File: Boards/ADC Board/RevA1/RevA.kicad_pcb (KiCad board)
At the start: 2 copper layers, 85 x 56 mm, 31 parts, among them J1 Left Connector, J10 Jumper Terminals, J11 Arduino Nano, J12 Arduino Nano, J13 Extra Pins, J14 Screw Terminals, J16 Screw Terminals, J2 Right Connector, J3 Screw Terminals, J4 Jumper Terminals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

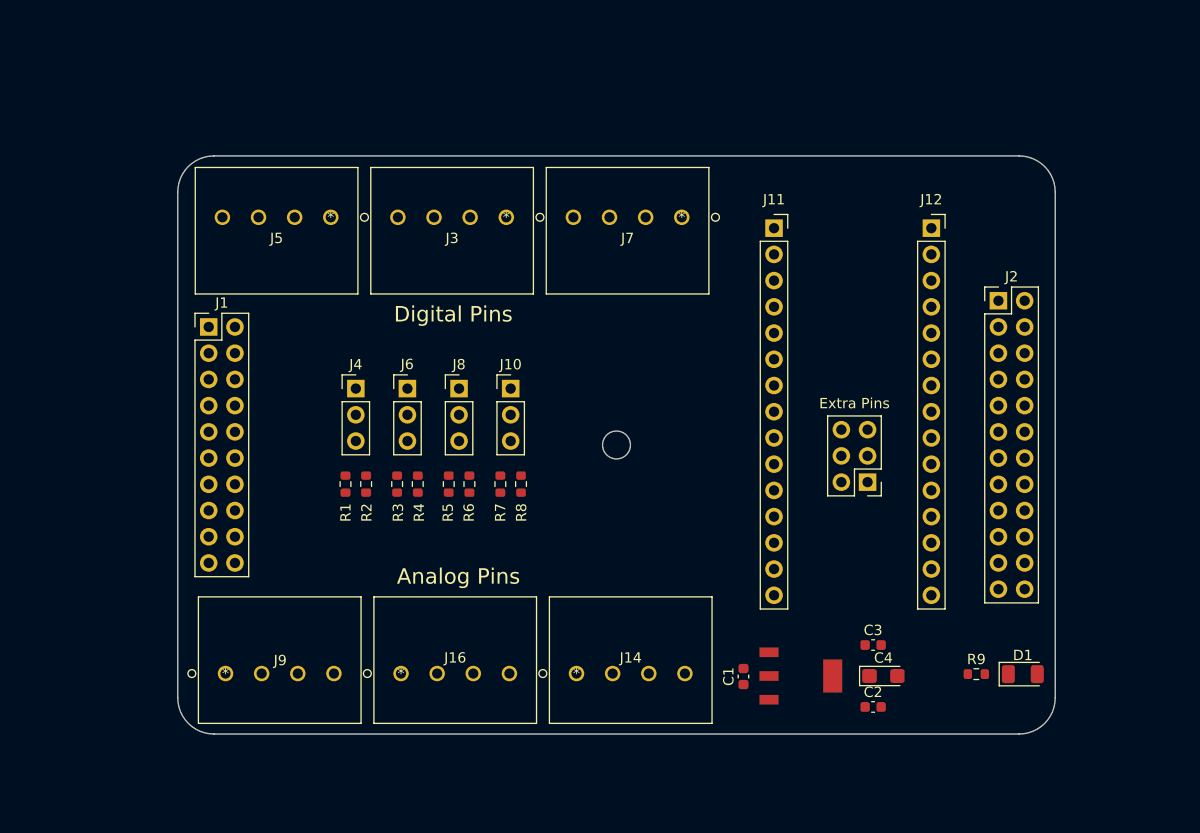
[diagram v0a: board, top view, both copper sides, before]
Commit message: Finished autorouting ADC board and placing text.
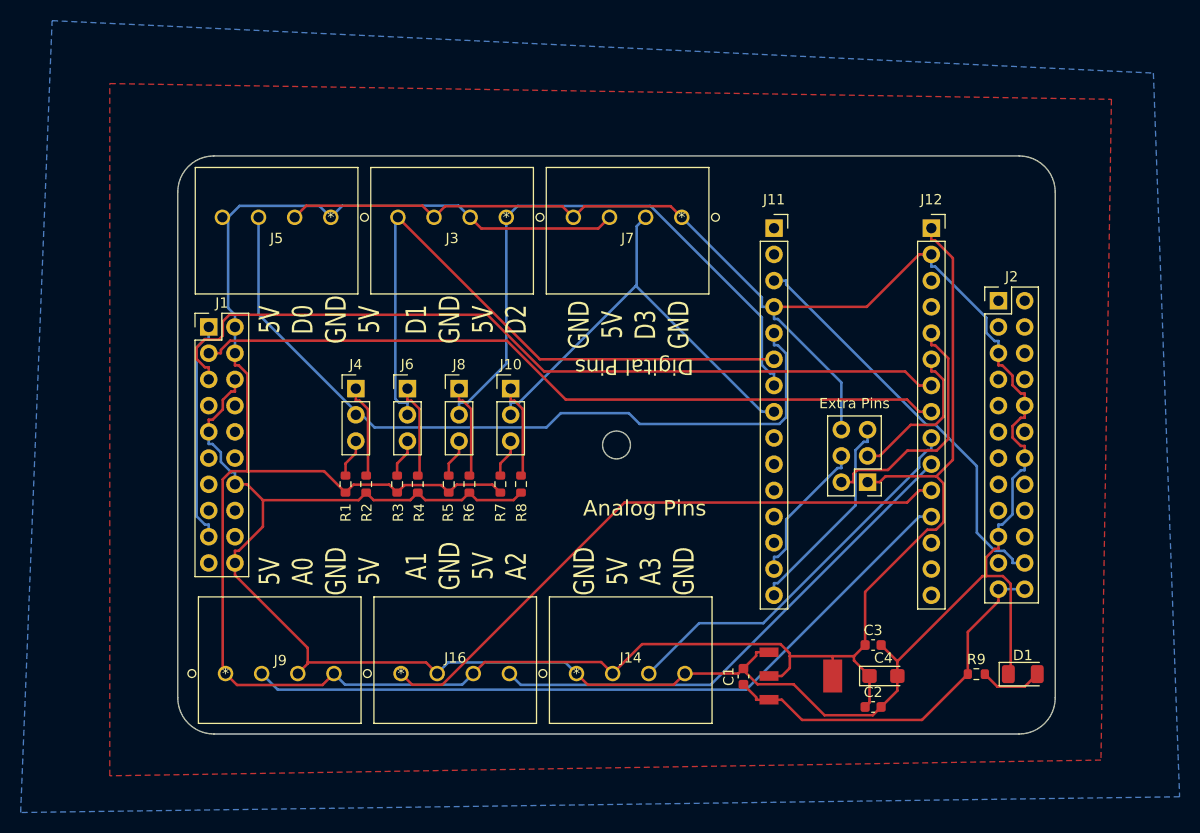
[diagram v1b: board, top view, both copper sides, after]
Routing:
- net /GND: track 0.00 -> 284.3 mm
- net /5V: track 0.00 -> 245.8 mm
- net /I2C_Clock: track 0.00 -> 79.9 mm
- net /Digital_0: track 0.00 -> 75.8 mm
- net /I2C_Data: track 0.00 -> 73.5 mm
- net /Analog_0: track 0.00 -> 72.5 mm
- net /Digital_1: track 0.00 -> 62.3 mm
- net /Analog_1: track 0.00 -> 59.6 mm
- net /Digital_2: track 0.00 -> 58.5 mm
- net /Analog_2: track 0.00 -> 50.2 mm
- net /Digital_3: track 0.00 -> 43.5 mm
- net /Reset: track 0.00 -> 39.8 mm
- net /Analog_3: track 0.00 -> 38.0 mm
- net /VCC: track 0.00 -> 37.1 mm
- net /Controller/A7: track 0.00 -> 23.7 mm
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- added copper zone on B.Cu, net /GND
- added copper zone on F.Cu, net /GND
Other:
- board text added: "5V"
- board text added: "5V A0 GND 5V"
- board text added: "5V D0 GND 5V"
- board text added: "A0"
- board text added: "A1"
- board text added: "A1 GND 5V A2"
- board text added: "A2"
- board text added: "A3"
- board text added: "D0"
- board text added: "D1"
- board text added: "D1 GND 5V D2"
- board text added: "D2"
- board text added: "D3"
- board text added: "GND"
- board text added: "GND 5V A3 GND"
- board text added: "GND 5V D3 GND"

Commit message: In process of updating ADC board to remove 5V connection from PI. Also commiting small changes to uV board.
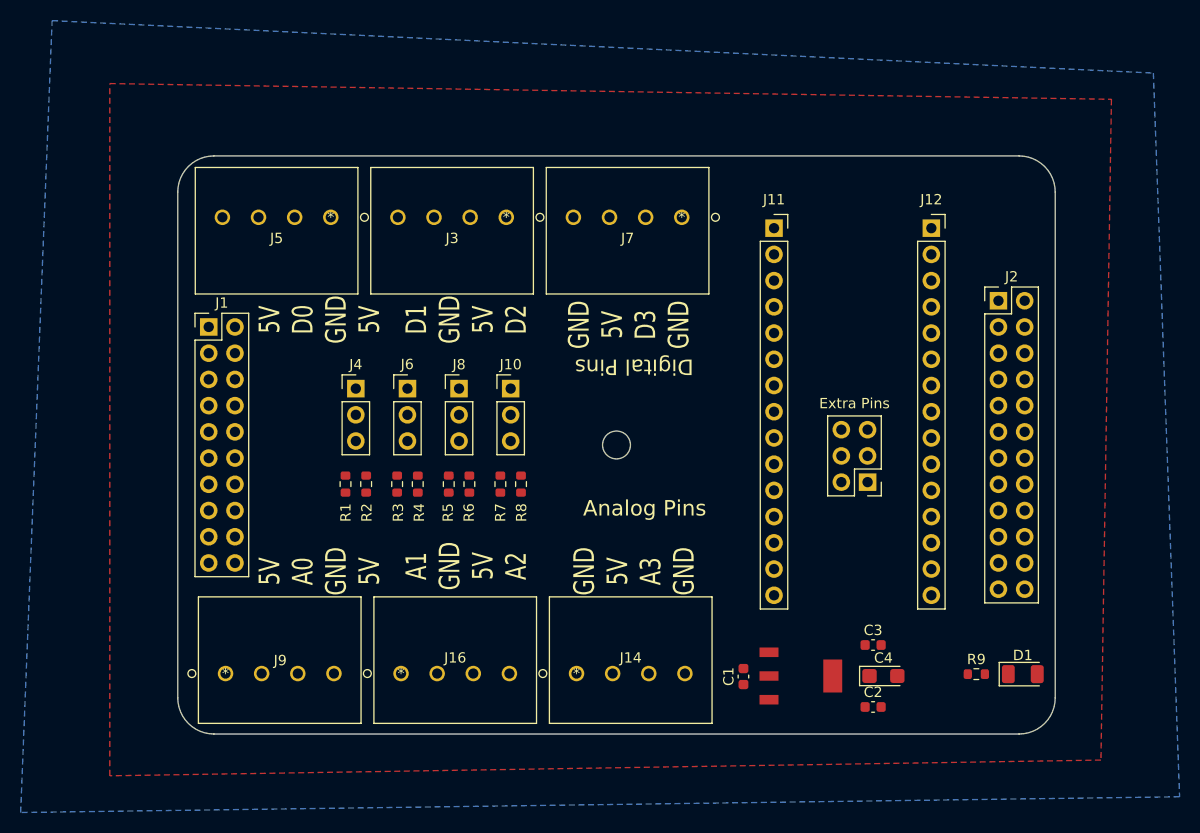
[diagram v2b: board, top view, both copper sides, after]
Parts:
- J11: value Arduino Nano -> Arduino Nano L
- J12: value Arduino Nano -> Arduino Nano R
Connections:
- J1 pad 2: /5V -> Net-(J1-Pad2)
- J1 pad 4: /5V -> Net-(J1-Pad4)
- J14 pad 2: /5V -> /Analog_0
- J14 pad 3: /Analog_3 -> /5V
- J14 pad 4: /GND -> (no net)
- J16 pad 1: /Analog_1 -> /GND
- J16 pad 2: /GND -> /Analog_2
- J16 pad 4: /Analog_2 -> (no net)
- J3 pad 1: /Digital_2 -> /GND
- J3 pad 2: /5V -> /Digital_0
- J3 pad 3: /GND -> /5V
- J3 pad 4: /Digital_1 -> (no net)
- J5 pad 1: /5V -> /GND
- J5 pad 2: /GND -> /Digital_1
- J5 pad 3: /Digital_0 -> /5V
- J5 pad 4: /5V -> (no net)
- J7 pad 2: /Digital_3 -> /Digital_2
- J7 pad 4: /GND -> (no net)
- J9 pad 1: /5V -> /GND
- J9 pad 2: /Analog_0 -> /Digital_3
- J9 pad 3: /GND -> /5V
- J9 pad 4: /5V -> (no net)
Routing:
- net /GND: track 284.3 -> 0.00 mm
- net /5V: track 245.8 -> 0.00 mm
- net /I2C_Clock: track 79.9 -> 0.00 mm
- net /Digital_0: track 75.8 -> 0.00 mm
- net /I2C_Data: track 73.5 -> 0.00 mm
- net /Analog_0: track 72.5 -> 0.00 mm
- net /Digital_1: track 62.3 -> 0.00 mm
- net /Analog_1: track 59.6 -> 0.00 mm
- net /Digital_2: track 58.5 -> 0.00 mm
- net /Analog_2: track 50.2 -> 0.00 mm
- net /Digital_3: track 43.5 -> 0.00 mm
- net /Reset: track 39.8 -> 0.00 mm
- net /Analog_3: track 38.0 -> 0.00 mm
- net /VCC: track 37.1 -> 0.00 mm
- net /Controller/A7: track 23.7 -> 0.00 mm
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
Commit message: Fixed associations between screw terminals and necessary pins. Updating ADC board to fix those PI pins.
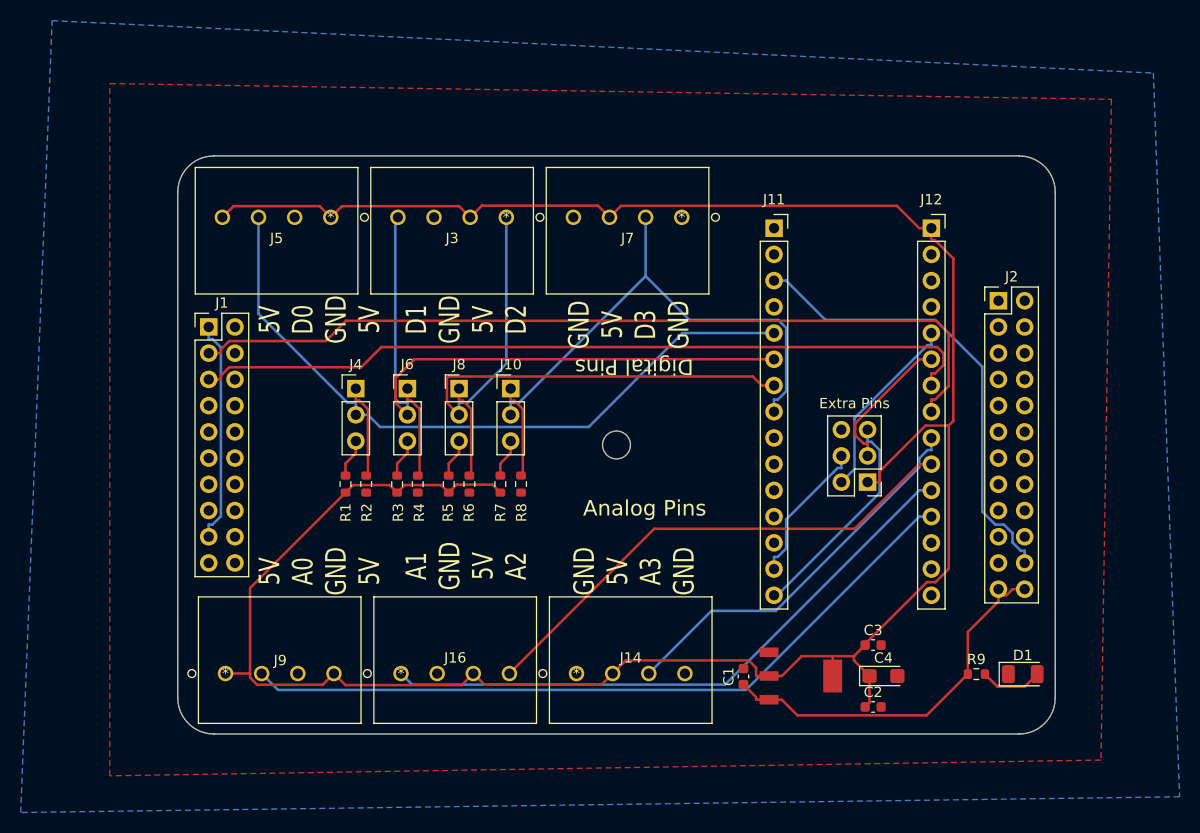
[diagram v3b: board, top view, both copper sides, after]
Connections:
- J14 pad 2: /Analog_0 -> /5V
- J14 pad 3: /5V -> /Analog_3
- J14 pad 4: (no net) -> /GND
- J16 pad 1: /GND -> /Analog_1
- J16 pad 2: /Analog_2 -> /GND
- J16 pad 4: (no net) -> /Analog_2
- J3 pad 1: /GND -> /Digital_2
- J3 pad 2: /Digital_0 -> /5V
- J3 pad 3: /5V -> /GND
- J3 pad 4: (no net) -> /Digital_1
- J5 pad 1: /GND -> /5V
- J5 pad 2: /Digital_1 -> /GND
- J5 pad 3: /5V -> /Digital_0
- J5 pad 4: (no net) -> /5V
- J7 pad 2: /Digital_2 -> /Digital_3
- J7 pad 4: (no net) -> /GND
- J9 pad 1: /GND -> /5V
- J9 pad 2: /Digital_3 -> /Analog_0
- J9 pad 3: /5V -> /GND
- J9 pad 4: (no net) -> /5V
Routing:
- net /5V: track 0.00 -> 242.6 mm
- net /I2C_Data: track 0.00 -> 82.2 mm
- net /I2C_Clock: track 0.00 -> 76.8 mm
- net /Analog_0: track 0.00 -> 72.5 mm
- net /Digital_0: track 0.00 -> 68.3 mm
- net /Digital_1: track 0.00 -> 61.7 mm
- net /Analog_1: track 0.00 -> 59.6 mm
- net /Digital_2: track 0.00 -> 57.7 mm
- net /Digital_3: track 0.00 -> 49.5 mm
- net /Analog_2: track 0.00 -> 49.3 mm
- net /Reset: track 0.00 -> 45.0 mm
- net /Analog_3: track 0.00 -> 38.0 mm
- net /VCC: track 0.00 -> 37.0 mm
- net /3.3V: track 0.00 -> 21.7 mm
- net /Controller/D12: track 0.00 -> 21.2 mm
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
